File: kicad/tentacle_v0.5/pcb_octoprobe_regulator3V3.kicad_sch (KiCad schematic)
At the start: 20 parts, among them U202 AMS1117-3.3, U204 TPS2595xx, U205 TPS2595xx, U206 MT9700

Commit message: ERC and DRC without errors and warnings LEDS less bright (Green LEDs 2k2 -> 4k7)
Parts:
- removed C218: 10u, Capacitor_SMD:C_0603_1608Metric, symbol 00_project_library:C
- removed R210: 12k, Resistor_SMD:R_0402_1005Metric, symbol Device:R
- removed U206: MT9700, Package_TO_SOT_SMD:SOT-23-5, symbol 00_project_library:MT9700
- added R212: 33K, Resistor_SMD:R_0402_1005Metric, symbol Device:R
- added U207: TPS2595xx, Package_SON:WSON-8-1EP_2x2mm_P0.5mm_EP0.9x1.6mm, symbol 00_project_library:TPS2595xx
- R103, R104: value 2k2 -> 4k7
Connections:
- net +3V3: now also U207.3 (VIN), U207.4 (VIN)
- net +3V3infra: now also U207.5 (OUT)
- net GND: now also R212.1, U207.8 (GND), U207.9 (GND)
- net RP2_INFRA_PWR_EN: now also U207.2 (EN/UVLO)
- new net: R212.2, U207.7 (ILIM)
- no-connect marks 2 -> 4
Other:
- note added: "Datasheet "Active Current Limiting": Goal: 100mA Rilm = 2000/(0.1A-0.04) = R33K333, choosen: R33K"
- note removed: "Datasheet Rset 12k corresponds to current limit of 0.5A"
- moved on the sheet: D104, R104

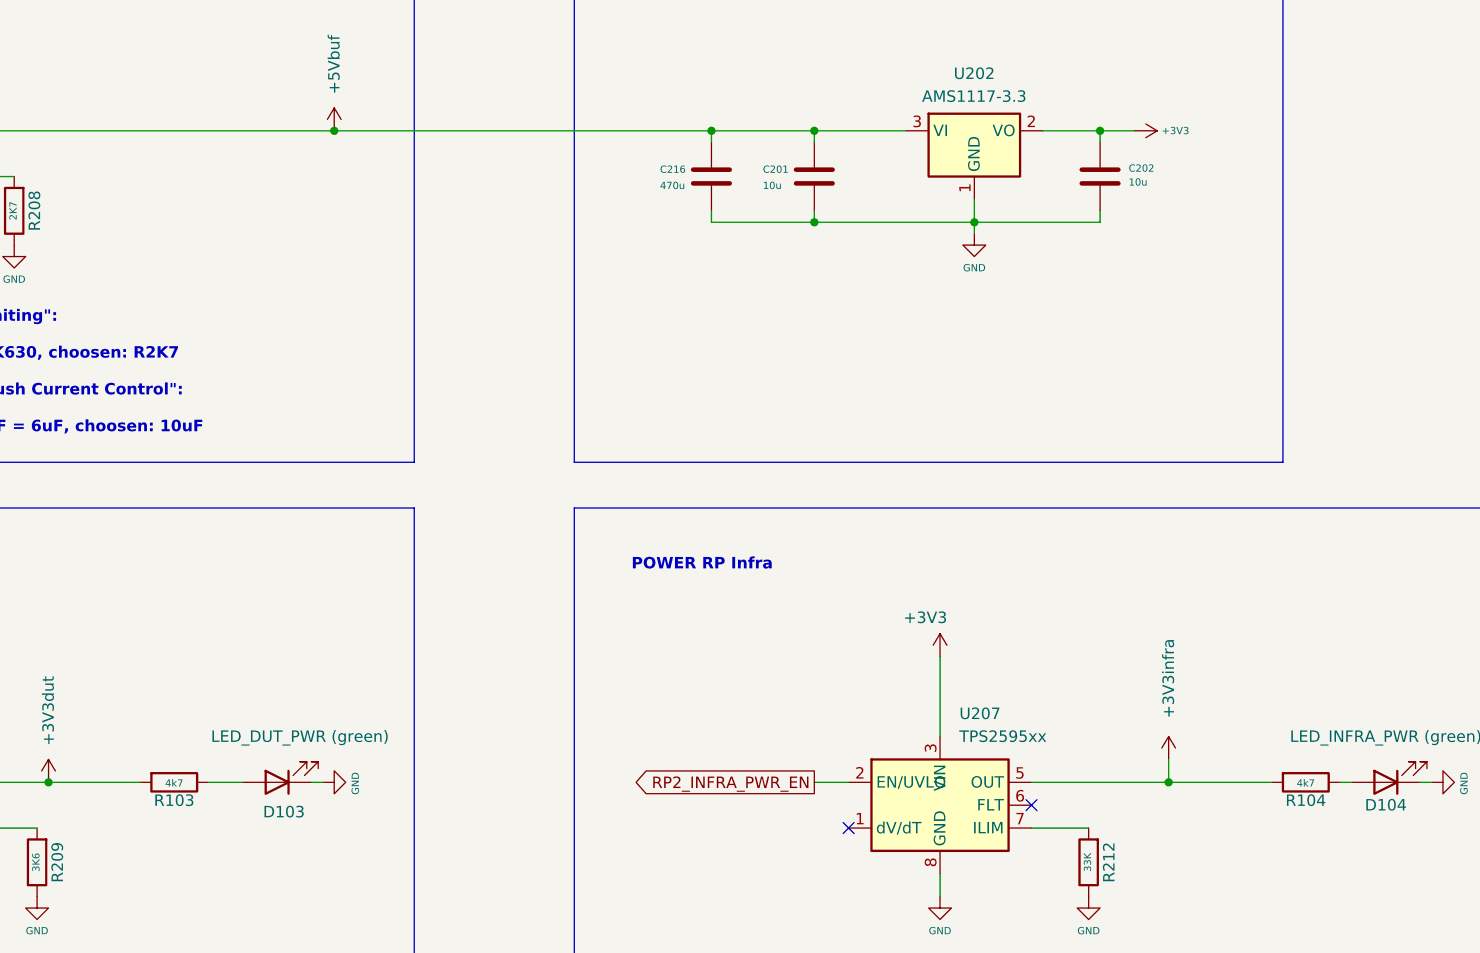
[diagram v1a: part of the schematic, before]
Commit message: Ordered tentacle v0.5 at jlcpcb
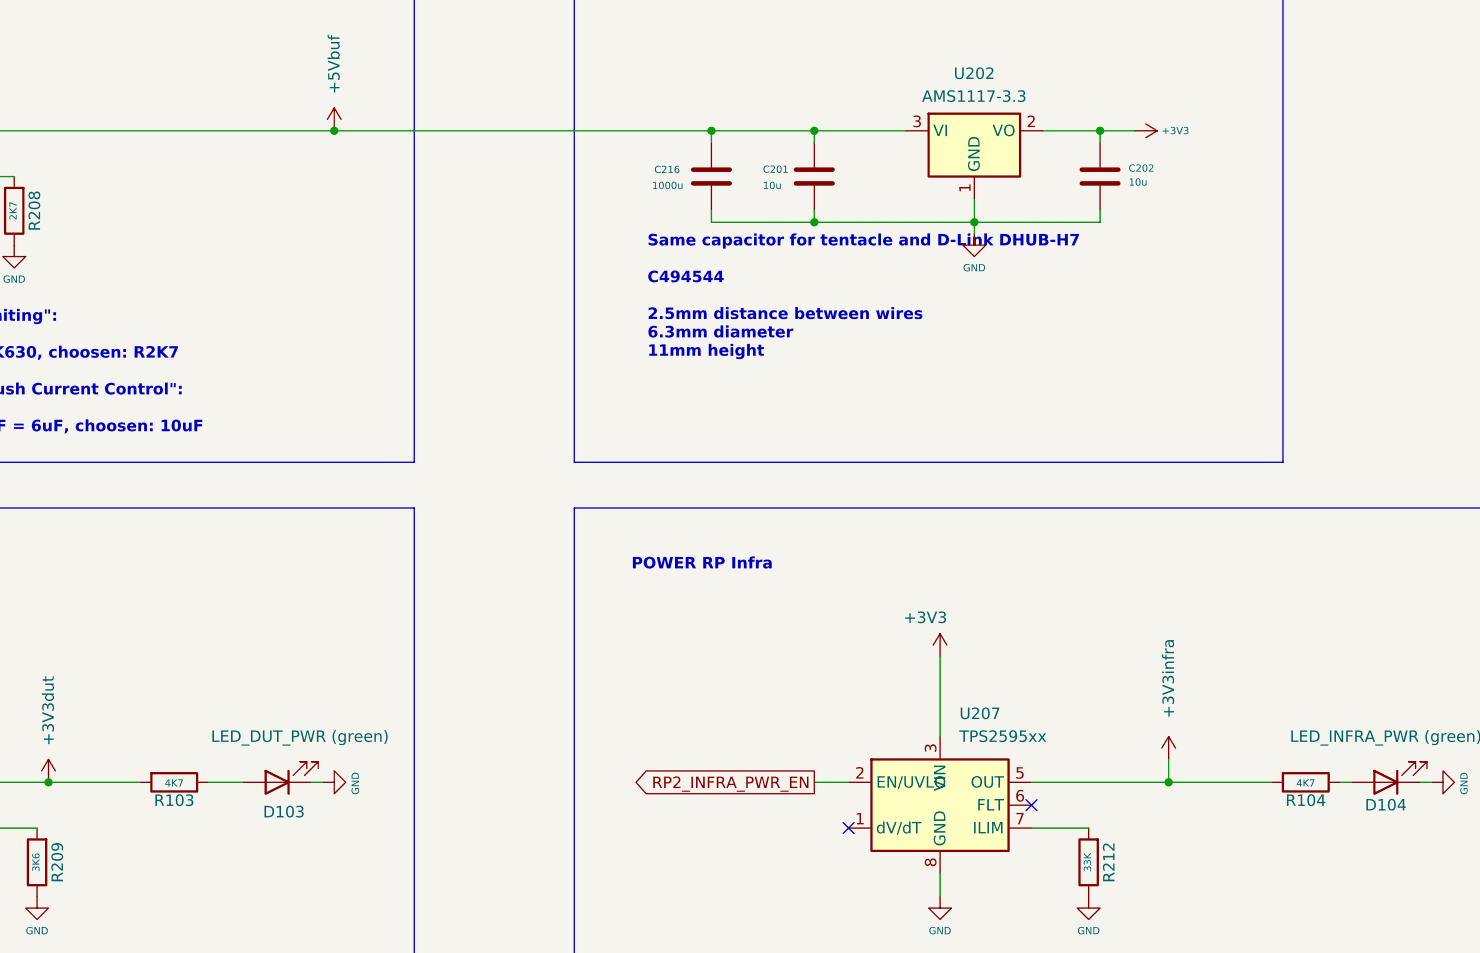
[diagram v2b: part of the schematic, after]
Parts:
- BP201, BP202: now left out of the parts list
- C216: value 470u -> 1000u; footprint Capacitor_SMD:C_Elec_6.3x5.8 -> Capacitor_THT:CP_Radial_D8.0mm_P2.50mm; JLC C7465562 -> C494544; now left out of the parts list
- R103, R104: value 4k7 -> 4K7
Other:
- note added: "Same capacitor for tentacle and D-Link DHUB-H7 C494544 2.5mm distance between wires 6.3mm diameter 11mm height"
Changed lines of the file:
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@@
 		)
 	)
+	(text "Same capacitor for tentacle and D-Link DHUB-H7\n\nC494544\n\n2.5mm distance between wires\n6.3mm diameter\n11mm height"
+		(exclude_from_sim no)
+		(at 163.068 63.5 0)
+		(effects
+			(font
+				(size 1.27 1.27)
+				(thickness 0.254)
+				(bold yes)
+			)
+			(justify left bottom)
+		)
+	)
 	(junction
 		(at 170.18 38.1)
@@
 			)
 		)
-		(property "Value" "4k7"
+		(property "Value" "4K7"
 			(at 110.49 110.5916 90)
 			(effects
@@
 		(unit 1)
 		(exclude_from_sim no)
-		(in_bom yes)
+		(in_bom no)
 		(on_board yes)
 		(dnp no)
@@
 		(unit 1)
 		(exclude_from_sim no)
-		(in_bom yes)
+		(in_bom no)
 		(on_board yes)
 		(dnp no)
@@
 			)
 		)
-		(property "Value" "4k7"
+		(property "Value" "4K7"
 			(at 236.22 110.5916 90)
 			(effects
@@
 		(unit 1)
 		(exclude_from_sim no)
-		(in_bom yes)
+		(in_bom no)
 		(on_board yes)
 		(dnp no)
 		(property "Reference" "C216"
-			(at 164.465 42.3926 0)
+			(at 163.83 42.418 0)
 			(effects
 				(font
@@
 			)
 		)
-		(property "Value" "470u"
-			(at 164.465 44.196 0)
+		(property "Value" "1000u"
+			(at 163.576 44.196 0)
 			(effects
 				(font
@@
 			)
 		)
-		(property "Footprint" "Capacitor_SMD:C_Elec_6.3x5.8"
+		(property "Footprint" "Capacitor_THT:CP_Radial_D8.0mm_P2.50mm"
 			(at 171.1452 46.99 0)
 			(effects
@@
 			)
 		)
-		(property "JLC" "C7465562"
+		(property "JLC" "C494544"
 			(at 133.3499 191.7701 0)
 			(effects
